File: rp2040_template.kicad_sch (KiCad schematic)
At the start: 37 parts, among them J1 USB_C_Receptacle_USB2.0_14P, J3 SWD, SW1 SW_BOOT, SW2 SW_BOOT, U1 RP2040, U2 W25Q16JVUXIQ TR, U3 AP2202K-3.3TRG1, Y1 ABM8-272-T3

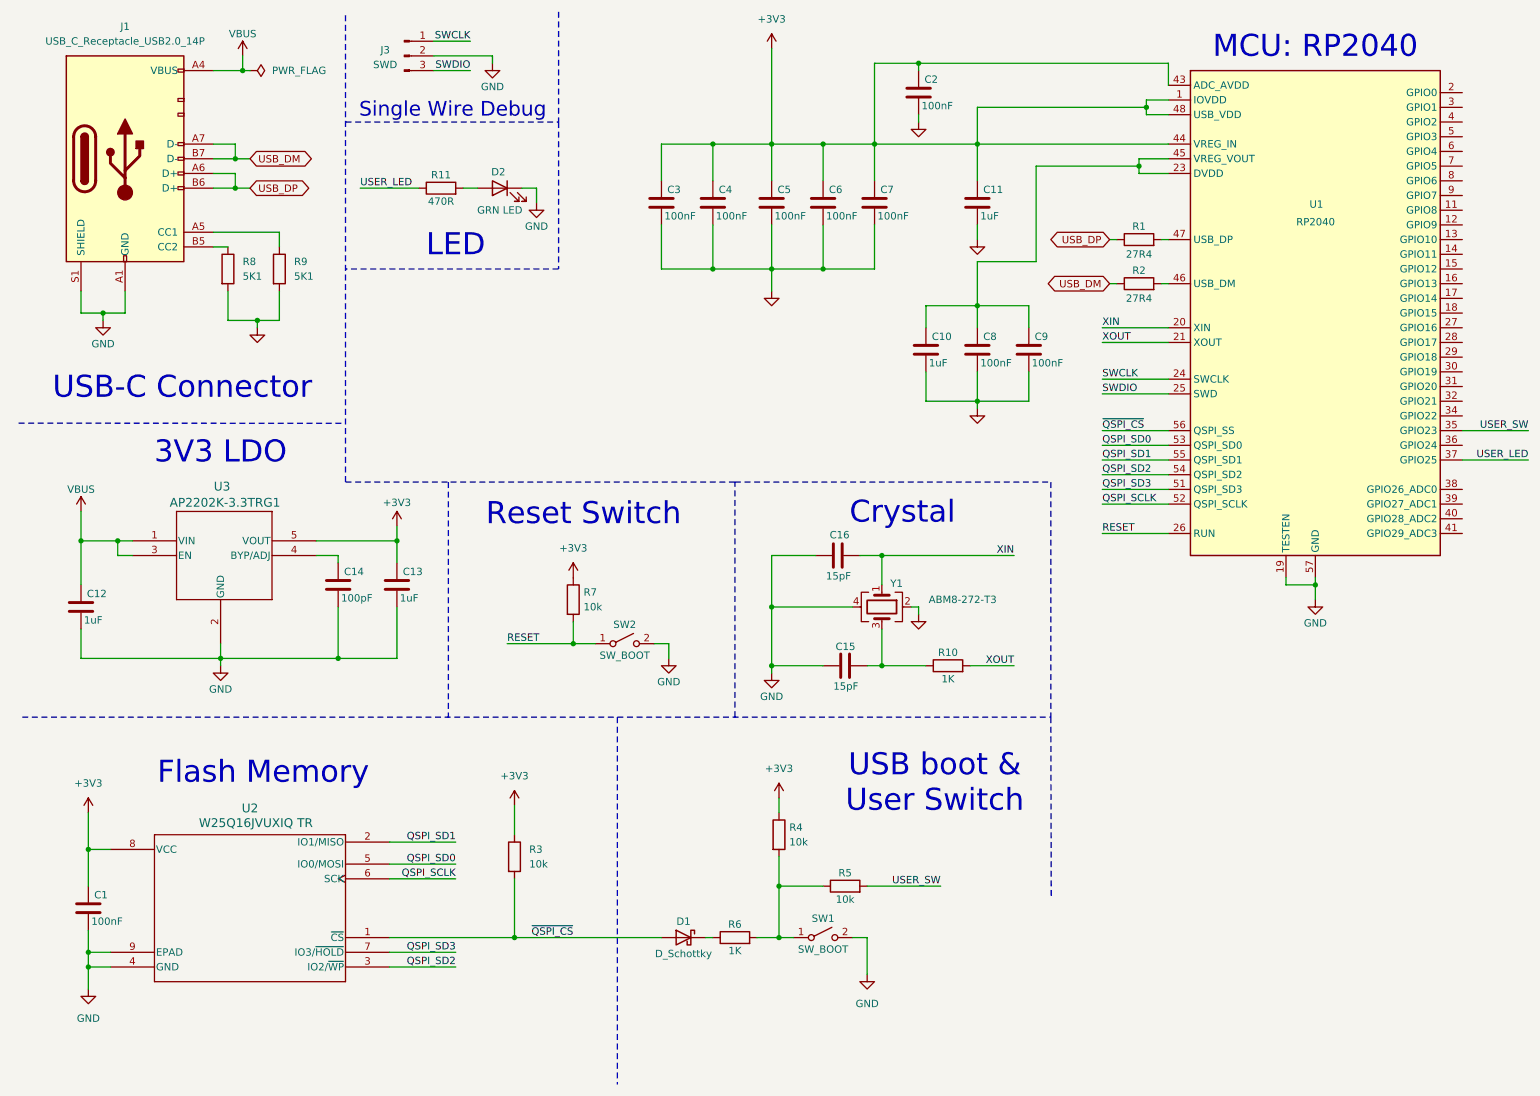
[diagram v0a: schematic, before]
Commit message: Added Footprints to components.
Signed-off-by Nathan <natelostintimeandspace@gmail.com>
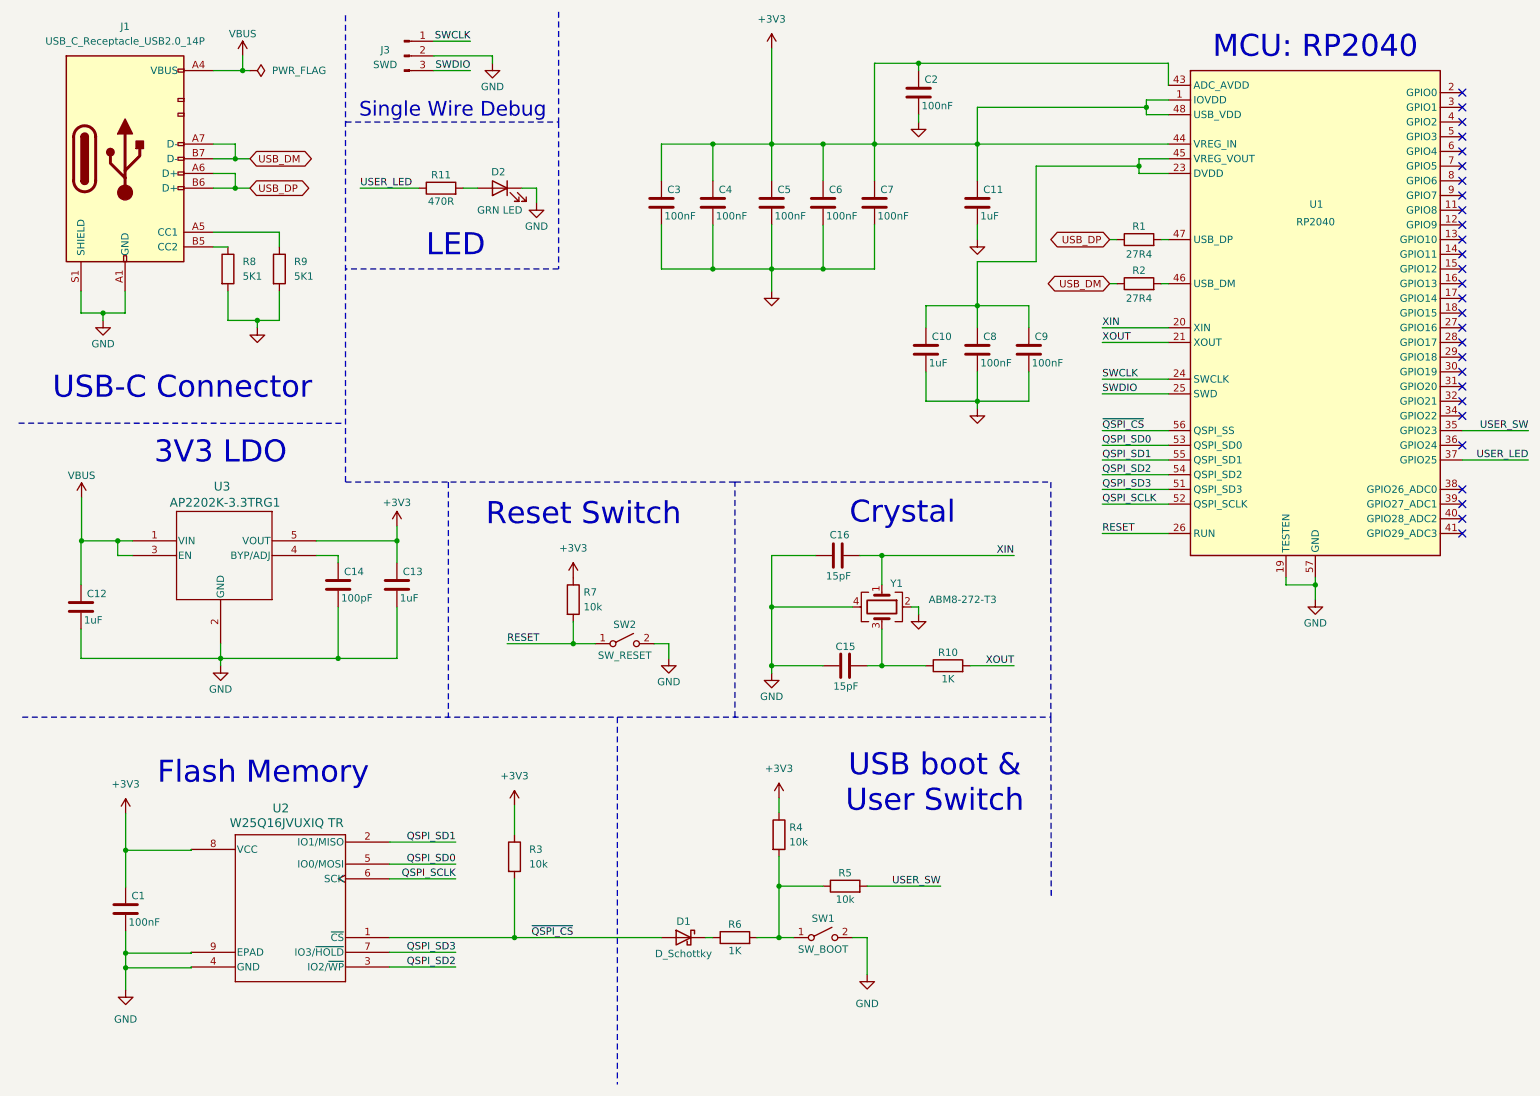
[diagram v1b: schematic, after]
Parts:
- C1, C10, C11, C12, C13, C14, C15, C16, C2, C3, C4, C5, C6, C7, C8, C9: footprint (none) -> Capacitor_SMD:C_0201_0603Metric
- D1: footprint (none) -> Diode_SMD:D_0603_1608Metric
- D2: footprint (none) -> LED_SMD:LED_0805_2012Metric
- J1: footprint (none) -> Connector_USB:USB_C_Receptacle_HRO_TYPE-C-31-M-12
- J3: footprint (none) -> Connector_PinHeader_2.54mm:PinHeader_1x03_P2.54mm_Vertical
- R1, R10, R11, R2, R3, R4, R5, R6, R7, R8, R9: footprint (none) -> Resistor_SMD:R_0201_0603Metric
- SW1: footprint (none) -> Button_Switch_SMD:SW_SPST_PTS810
- SW2: value SW_BOOT -> SW_RESET; footprint (none) -> Button_Switch_SMD:SW_SPST_PTS810
- U2: footprint USON-8_UX_2x3x0p6_WIN -> footprints:USON-8_UX_2x3x0p6_WIN
- U3: footprint SOT-23-5_AP2202_DIO -> footprints:SOT-23-5_AP2202_DIO
- Y1: value ABM8-272-T3 -> ABM8-272-T3; footprint (none) -> Crystal:Crystal_SMD_2520-4Pin_2.5x2.0mm
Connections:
- net +3V3: now also U1.10 (IOVDD), U1.22 (IOVDD), U1.33 (IOVDD), U1.42 (IOVDD), U1.49 (IOVDD), U1.50 (DVDD)
- no-connect marks 0 -> 28
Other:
- moved on the sheet: C1, U2

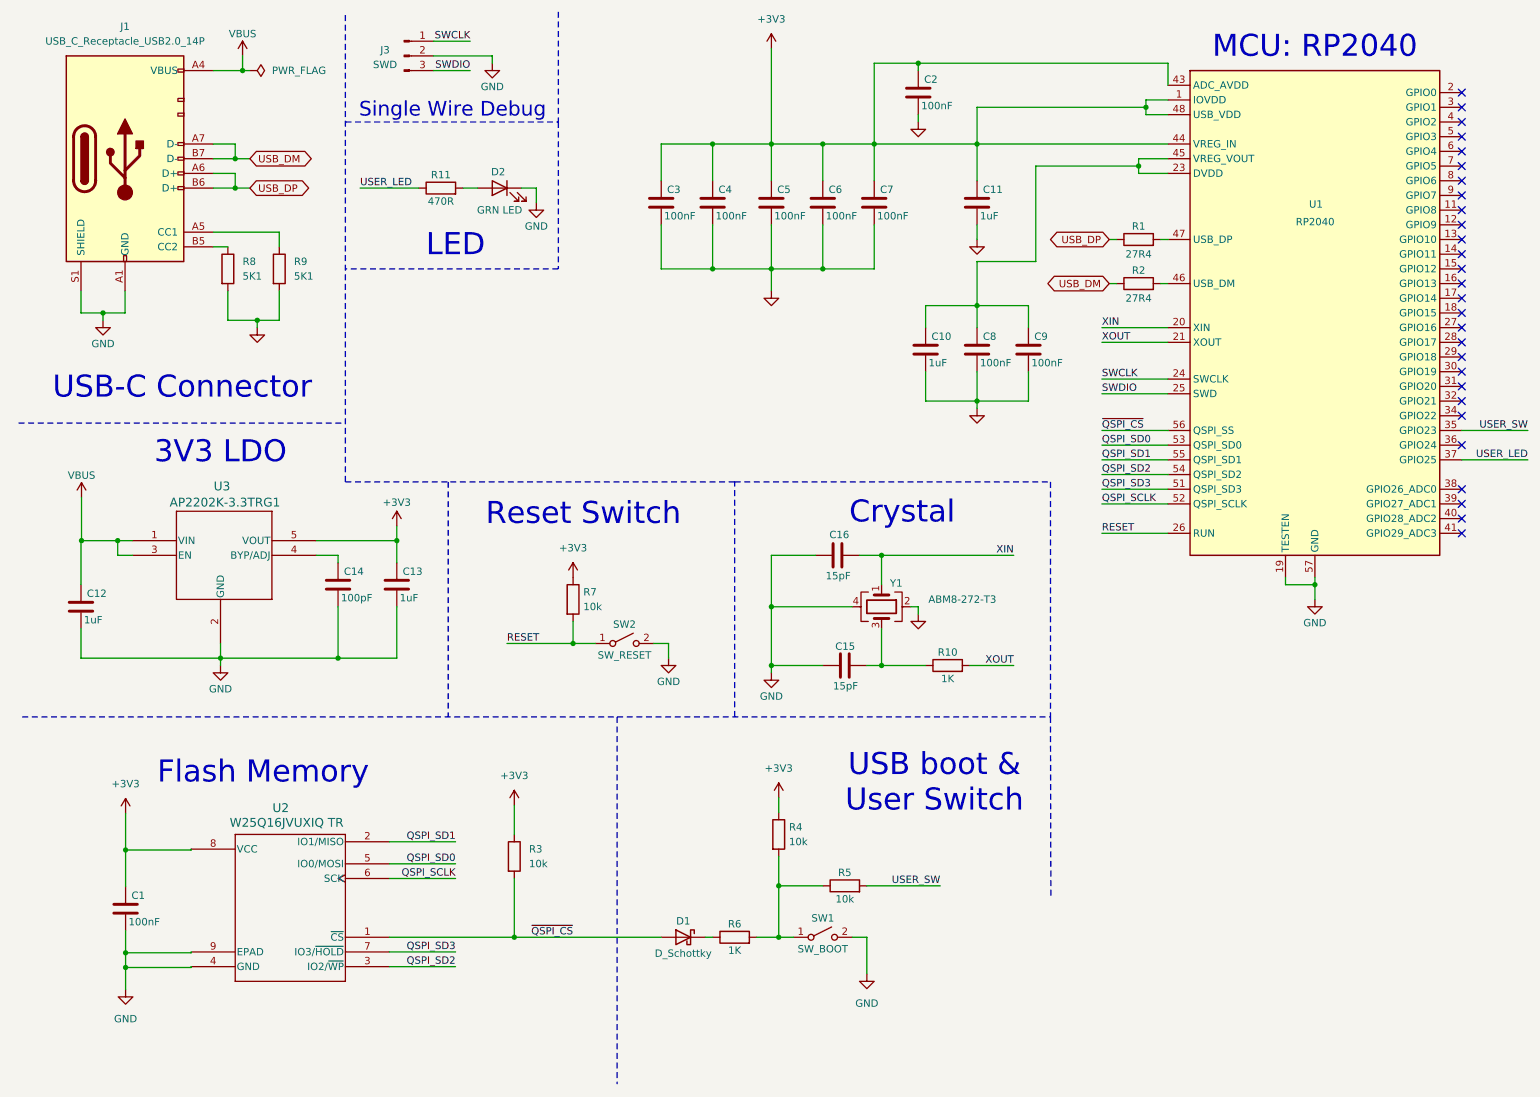
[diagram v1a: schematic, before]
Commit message: Added castellated edges to PCB. began work on layout.
Signed-off-by: Nate <natelostintimeandspace@gmail.com>
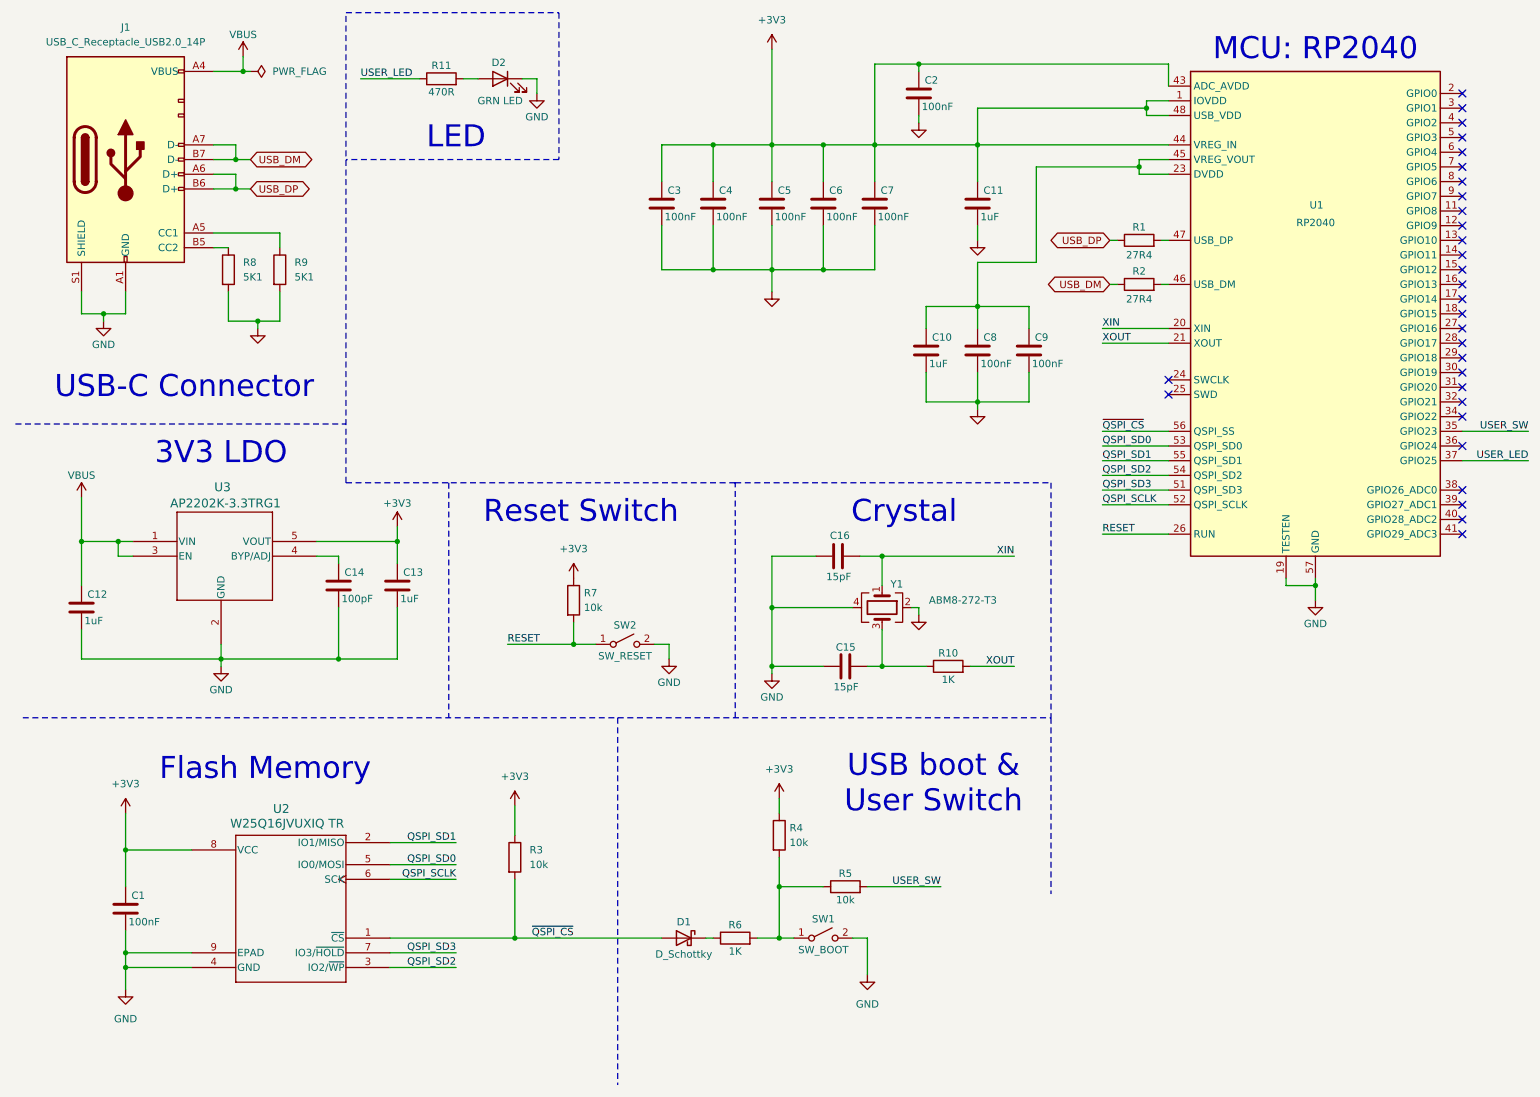
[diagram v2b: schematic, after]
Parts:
- removed J3: SWD, Connector_PinHeader_2.54mm:PinHeader_1x03_P2.54mm_Vertical, symbol Connector:Conn_01x03_Pin
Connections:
- net SWCLK: no longer names the net of U1.24 (SWCLK)
- net SWDIO: no longer names the net of U1.25 (SWD)
- no-connect marks 28 -> 30
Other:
- note removed: "Single Wire Debug"
- moved on the sheet: D2, R11

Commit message: Finished Rev A!
Signed-off-by: Nate <natelostintimeandspace@gmail.com>
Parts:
- removed U1: RP2040, Package_DFN_QFN:QFN-56-1EP_7x7mm_P0.4mm_EP3.2x3.2mm, symbol MCU_RaspberryPi:RP2040
- added C17: 100nF, Capacitor_SMD:C_01005_0402Metric, symbol Device:C
- added D3: D_Schottky, Diode_SMD:Nexperia_CFP3_SOD-123W, symbol Device:D_Schottky
- added FID1, FID2: Fiducial, Fiducial:Fiducial_0.5mm_Mask1mm, symbol Mechanical:Fiducial
- added J2, J3: Conn_01x20_Pin, castellated:castellated_tht_1x20, symbol Connector:Conn_01x20_Pin
- added J4: Conn_01x03_Pin, castellated:castellated_tht_1x3, symbol Connector:Conn_01x03_Pin
- added U4: RP2040, Package_DFN_QFN:QFN-56-1EP_7x7mm_P0.4mm_EP3.2x3.2mm, symbol MCU_RaspberryPi_RP2040:RP2040
- C1, C10, C11, C12, C13, C14, C15, C16, C3, C4, C5, C6, C7, C8, C9: footprint Capacitor_SMD:C_0201_0603Metric -> Capacitor_SMD:C_01005_0402Metric
- D1: footprint Diode_SMD:D_0603_1608Metric -> Diode_SMD:D_01005_0402Metric
- LED1: renamed from D2; footprint LED_SMD:LED_0805_2012Metric -> LED_SMD:LED_0402_1005Metric_Pad0.77x0.64mm_HandSolder
- SW_1: renamed from SW1; value SW_BOOT -> BOOTSEL
- SW_2: renamed from SW2; value SW_RESET -> RESET
- U2: footprint footprints:USON-8_UX_2x3x0p6_WIN -> Package_SON:Winbond_USON-8-1EP_3x2mm_P0.5mm_EP0.2x1.6mm
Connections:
- net +3V3: now also C8.1, C9.1, C17.1, J3.5 (Pin_5), U4.1 (IOVDD), U4.10 (IOVDD), U4.22 (IOVDD), U4.33 (IOVDD), U4.42 (IOVDD), U4.43 (ADC_AVDD), U4.44 (VREG_IN), U4.48 (USB_VDD), U4.49 (IOVDD); no longer C6.1, C7.1
- net GND: now also C17.2, J2.13 (Pin_13), J2.18 (Pin_18), J2.3 (Pin_3), J2.8 (Pin_8), J3.13 (Pin_13), J3.18 (Pin_18), J3.3 (Pin_3), J3.8 (Pin_8), J4.2 (Pin_2), U4.19 (TESTEN), U4.57 (GND)
- net QSPI_SCLK: now also U4.52 (QSPI_SCLK)
- net QSPI_SD0: now also U4.53 (QSPI_SD0)
- net QSPI_SD1: now also U4.55 (QSPI_SD1)
- net QSPI_SD2: now also U4.54 (QSPI_SD2)
- net QSPI_SD3: now also U4.51 (QSPI_SD3)
- net RESET: now also U4.26 (RUN)
- net USER_LED: now also U4.37 (GPIO25)
- net USER_SW: now also U4.35 (GPIO23)
- net VBUS: now also D3.2 (A), J3.1 (Pin_1); no longer C12.1, U3.1 (VIN), U3.3 (EN)
- net XIN: now also U4.20 (XIN)
- net XOUT: now also U4.21 (XOUT)
- net ~{QSPI_CS}: now also U4.56 (QSPI_SS)
- net at R1.2: now also U4.47 (USB_DP)
- net at R2.2: now also U4.46 (USB_DM)
- new net +1V1: C10.1, C6.1, C7.1, U4.23 (DVDD), U4.45 (VREG_VOUT), U4.50 (DVDD)
- new net ADC0: J3.10 (Pin_10), U4.38 (GPIO26_ADC0)
- new net ADC1: J3.9 (Pin_9), U4.39 (GPIO27_ADC1)
- new net ADC2: J3.7 (Pin_7), U4.40 (GPIO28_ADC2)
- new net ADC3: J3.6 (Pin_6), U4.41 (GPIO29_ADC3)
- new net GPIO0: J2.1 (Pin_1), U4.2 (GPIO0)
- new net GPIO1: J2.2 (Pin_2), U4.3 (GPIO1)
- new net GPIO10: J2.14 (Pin_14), U4.13 (GPIO10)
- new net GPIO11: J2.15 (Pin_15), U4.14 (GPIO11)
- new net GPIO12: J2.16 (Pin_16), U4.15 (GPIO12)
- new net GPIO13: J2.17 (Pin_17), U4.16 (GPIO13)
- new net GPIO14: J2.19 (Pin_19), U4.17 (GPIO14)
- new net GPIO15: J2.20 (Pin_20), U4.18 (GPIO15)
- new net GPIO16: J3.20 (Pin_20), U4.27 (GPIO16)
- new net GPIO17: J3.19 (Pin_19), U4.28 (GPIO17)
- new net GPIO18: J3.17 (Pin_17), U4.29 (GPIO18)
- new net GPIO19: J3.16 (Pin_16), U4.30 (GPIO19)
- new net GPIO2: J2.4 (Pin_4), U4.4 (GPIO2)
- new net GPIO20: J3.15 (Pin_15), U4.31 (GPIO20)
- new net GPIO21: J3.14 (Pin_14), U4.32 (GPIO21)
- new net GPIO22: J3.12 (Pin_12), U4.34 (GPIO22)
- new net GPIO24: J3.11 (Pin_11), U4.36 (GPIO24)
- new net GPIO3: J2.5 (Pin_5), U4.5 (GPIO3)
- new net GPIO4: J2.6 (Pin_6), U4.6 (GPIO4)
- new net GPIO5: J2.7 (Pin_7), U4.7 (GPIO5)
- new net GPIO6: J2.9 (Pin_9), U4.8 (GPIO6)
- new net GPIO7: J2.10 (Pin_10), U4.9 (GPIO7)
- new net GPIO8: J2.11 (Pin_11), U4.11 (GPIO8)
- new net GPIO9: J2.12 (Pin_12), U4.12 (GPIO9)
- new net SWCLK: J4.3 (Pin_3), U4.24 (SWCLK)
- new net SWDIO: J4.1 (Pin_1), U4.25 (SWD)
- new net VSYS: C12.1, D3.1 (K), J3.2 (Pin_2), U3.1 (VIN), U3.3 (EN)
- no-connect marks 30 -> 1
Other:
- note added: "IO"
- note added: "SWD HEADER"
- note added: "USB-C CONNECTOR"
- note added: "VSYS POWER"
- note removed: "USB-C Connector"
- company: (none) -> Lost in Time and Space Electronics
- title: (none) -> RP2040 Template
- moved on the sheet: C1, C10, C11, C12, C13, C14, C15, C16, C2, C3, C4, C5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
